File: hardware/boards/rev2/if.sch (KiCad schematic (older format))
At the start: 60 parts, among them U39 ADA4940-2, U41 ADA4940-2

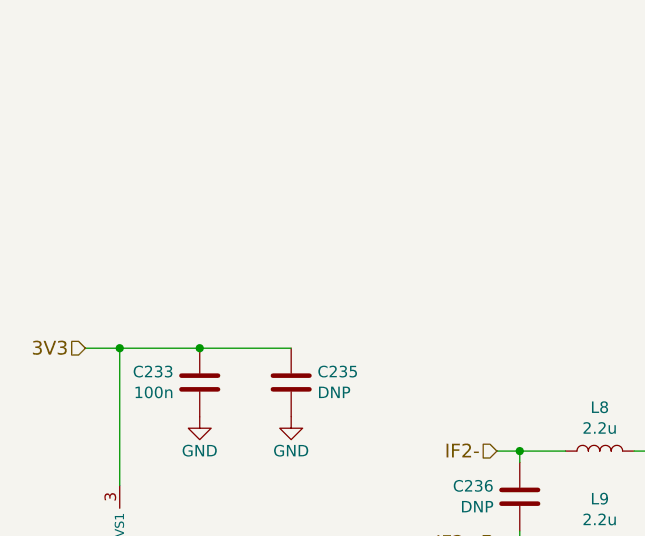
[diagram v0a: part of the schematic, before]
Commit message: reorganize schematic
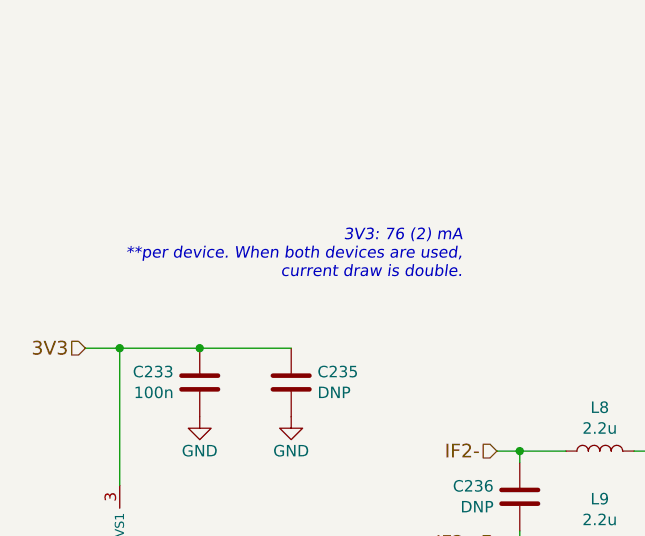
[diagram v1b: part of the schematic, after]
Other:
- note added: "3V3: 76 (2) mA\n**per device. When both devices are used,\ncurrent draw is double."

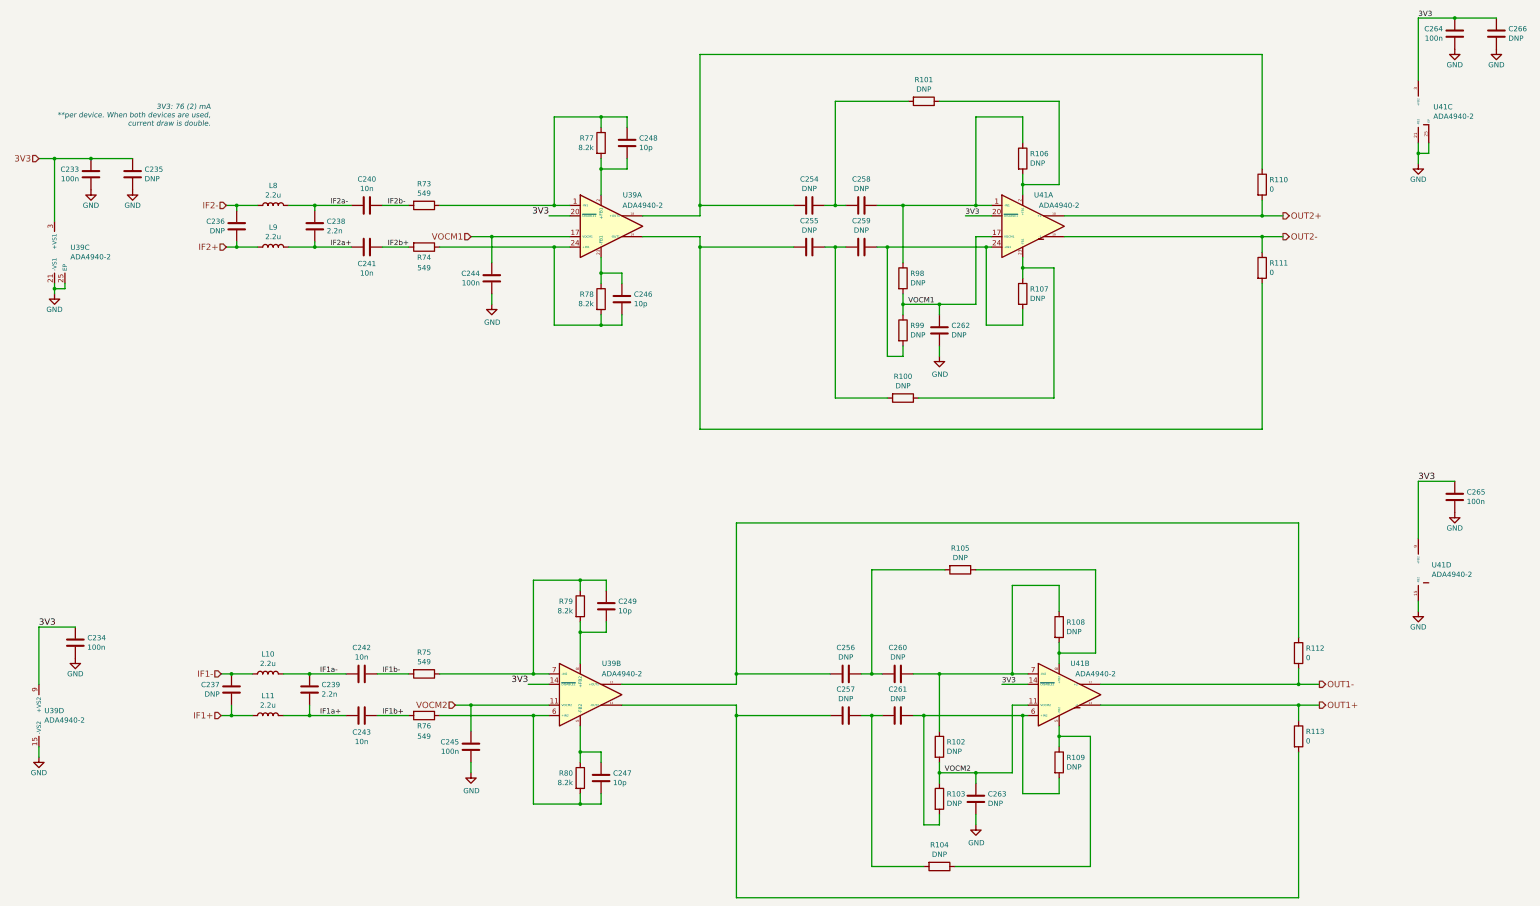
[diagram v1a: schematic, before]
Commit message: revert to kicad v5 for pcb gen
V6 contains a few bugs and a V6 board cannot be edited with V5.
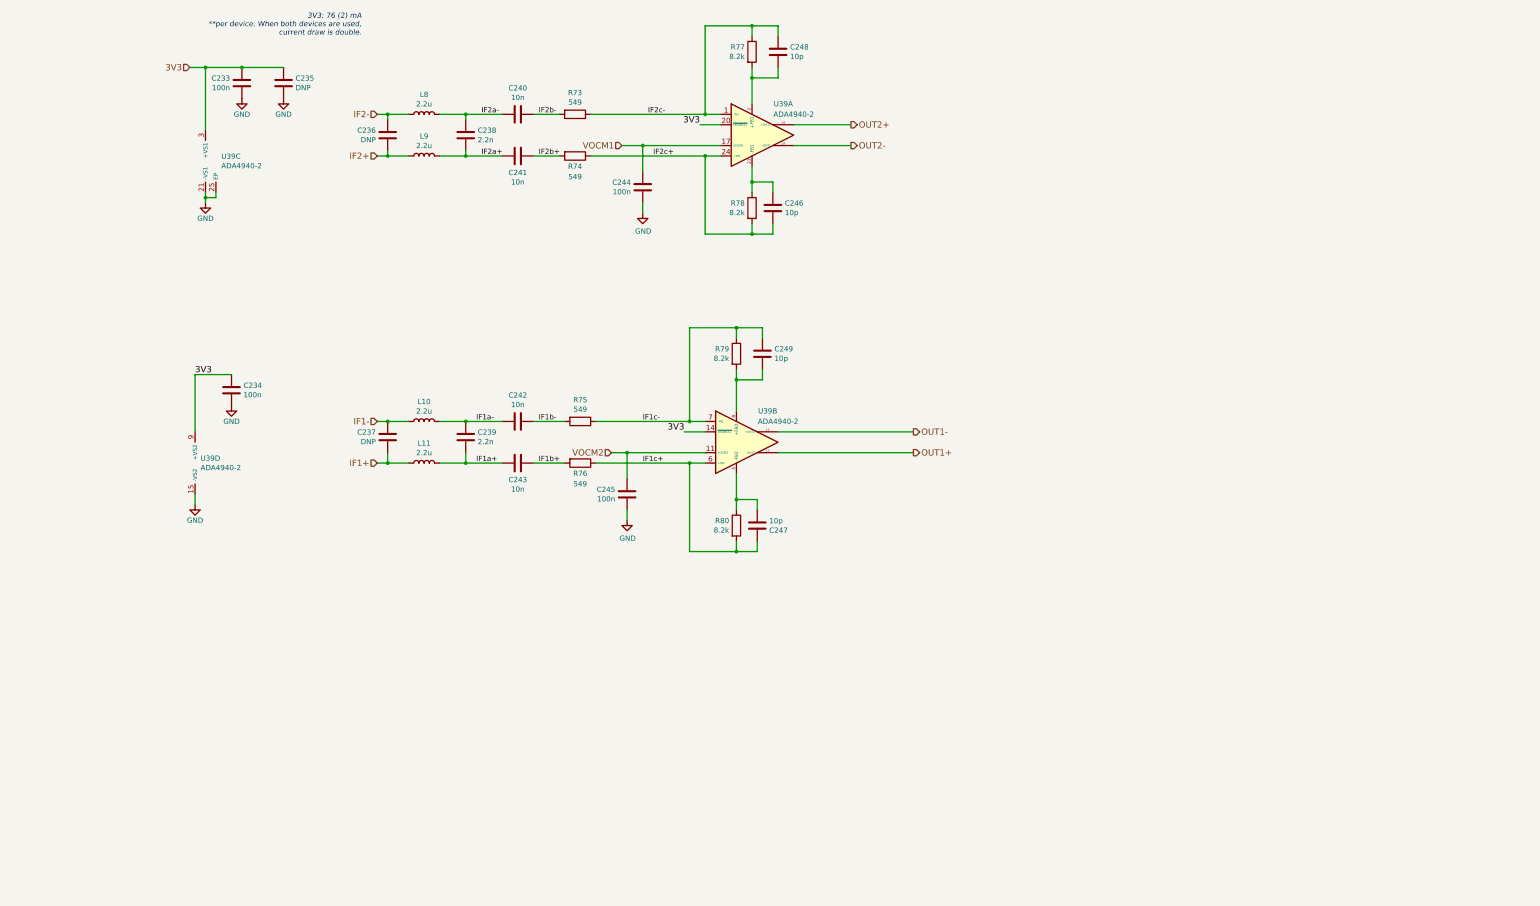
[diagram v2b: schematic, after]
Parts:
- removed C254, C255, C256, C257, C258, C259, C260, C261, C262, C263: DNP, Capacitor_SMD:C_0402_1005Metric, symbol Device:C
- removed C264, C265: 100n, Capacitor_SMD:C_0402_1005Metric, symbol Device:C
- removed C266: DNP, Capacitor_SMD:C_0805_2012Metric, symbol Device:C
- removed R100, R101, R102, R103, R104, R105, R106, R107, R108, R109, R98, R99: DNP, Resistor_SMD:R_0402_1005Metric, symbol Device:R
- removed R110, R111, R112, R113: 0, Resistor_SMD:R_0402_1005Metric, symbol Device:R
- removed U41: ADA4940-2, Package_CSP:LFCSP-24-1EP_4x4mm_P0.5mm_EP2.5x2.5mm, symbol Amplifier_Difference:ADA4940-2
- L10, L11, L8, L9: footprint Inductor_SMD:L_0805_2012Metric -> Inductor_SMD:L_0603_1608Metric; MFN LQM21PN2R2MC0D -> LQM18PN2R2MGHD
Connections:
- net OUT1+: now also U39.13 (-OUT2)
- net OUT1-: now also U39.12 (+OUT2)
- net OUT2+: now also U39.18 (+OUT1)
- net OUT2-: now also U39.19 (-OUT1)
- net IF1c-: now reaches C249.1, R75.1, R79.1, U39.7 (-IN2)
- net at R80.1, U39.5 (-FB2): now also C247.2; no longer C247.1
- net IF1c+: now reaches R76.1, R80.2, U39.6 (+IN2)
- net IF1c+: now also C247.1; no longer C247.2
- net IF2c-: now reaches C248.1, R73.1, R77.1, U39.1 (-IN1)
- net IF2c+: now reaches C246.2, R74.1, R78.2, U39.24 (+IN1)
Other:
- moved on the sheet: C233, C234, C235, C236, C237, C238, C239, C240, C241, C242, C243, C244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
